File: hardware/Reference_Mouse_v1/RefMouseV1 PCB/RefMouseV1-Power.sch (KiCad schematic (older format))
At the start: 9 parts, among them U1 TPS6205X

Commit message: More reference mouse pcb stuff
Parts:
- added JP2: M02PTH, SparkFun-1X02, symbol M02PTH
- added TP3: TEST-POINT3X5, SparkFun-PAD.03X.05, symbol TEST-POINT3X5
- gave numbers to parts that had none: 3
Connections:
- wire segments 42 -> 37
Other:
- note added: "+3.3V test point"
- note added: "0.1" header footprint for alternate\nconnectors, measurement, or charging."
- note added: "Always-on battery voltage"
- note added: "Bend and solder a clipped component lead here\nfor use as an alligator-clipable GND test point."
- note added: "Main power switch.\nEnables main regulators and\nmotor drivers. Does not need to\nbe rated for very much current."
- note added: "Mechanically switched battery voltage.\nNot for high-current loads."
- note added: "Polarized JST-XH\nLiPo balance connector"
- note added: "Regulated high-current 3.3V supply"
- moved on the sheet: M1
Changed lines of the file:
@@
 Sheet 2 2
 Title "TPS6205x-based Fixed Voltage Switching Regulator Module"
-Date "26 aug 2013"
+Date "30 aug 2013"
 Rev "A"
 Comp "UCR Micromouse"
@@
 $EndComp
 $Comp
-L GND #PWR08
+L GND #PWR03
 U 1 1 51E3374F
 P 2600 2500
-F 0 "#PWR08" H 2600 2500 30  0001 C CNN
+F 0 "#PWR03" H 2600 2500 30  0001 C CNN
 F 1 "GND" H 2600 2430 30  0001 C CNN
 F 2 "" H 2600 2500 60  0000 C CNN
@@
 $EndComp
 $Comp
-L GND #PWR09
+L GND #PWR04
 U 1 1 51E33C6A
 P 6150 2600
-F 0 "#PWR09" H 6150 2600 30  0001 C CNN
+F 0 "#PWR04" H 6150 2600 30  0001 C CNN
 F 1 "GND" H 6150 2530 30  0001 C CNN
 F 2 "" H 6150 2600 60  0000 C CNN
@@
 $EndComp
 $Comp
-L GND #PWR012
+L GND #PWR05
 U 1 1 51E34F59
 P 6450 3150
-F 0 "#PWR012" H 6450 3150 30  0001 C CNN
+F 0 "#PWR05" H 6450 3150 30  0001 C CNN
 F 1 "GND" H 6450 3080 30  0001 C CNN
 F 2 "" H 6450 3150 60  0000 C CNN
@@
 NoConn ~ 5100 2700
 $Comp
-L SWITCH-SPSTPTH S?
+L SWITCH-SPSTPTH S1
 U 1 1 521A8FC9
 P 2200 3700
-F 0 "S?" H 2150 3950 50  0000 L BNN
+F 0 "S1" H 2150 3950 50  0000 L BNN
 F 1 "SWITCH-SPSTPTH" H 2150 3450 50  0000 L BNN
 F 2 "SparkFun-SWITCH-SPDT" H 2500 3400 50  0001 C CNN
@@
 $EndComp
 $Comp
-L BATTBALANCE-2S M?
+L BATTBALANCE-2S M1
 U 1 1 521AAB8A
-P 900 2200
-F 0 "M?" H 800 2400 60  0000 C CNN
-F 1 "BATTBALANCE-2S" H 1125 1975 60  0000 C CNN
-F 2 "" H 950 2200 60  0000 C CNN
-F 3 "" H 950 2200 60  0000 C CNN
-	1    900  2200
-	1    0    0    -1
-$EndComp
-$Comp
-L GND #PWR?
+P 950 2200
+F 0 "M1" H 850 2400 60  0000 C CNN
+F 1 "BATTBALANCE-2S" H 1175 1975 60  0000 C CNN
+F 2 "" H 1000 2200 60  0000 C CNN
+F 3 "" H 1000 2200 60  0000 C CNN
+	1    950  2200
+	1    0    0    -1
+$EndComp
+$Comp
+L GND #PWR06
 U 1 1 521AABA6
 P 1600 2500
-F 0 "#PWR?" H 1600 2500 30  0001 C CNN
+F 0 "#PWR06" H 1600 2500 30  0001 C CNN
 F 1 "GND" H 1600 2430 30  0001 C CNN
 F 2 "" H 1600 2500 60  0000 C CNN
@@
 	1    0    0    -1
 $EndComp
-Wire Wire Line
-	5100 2100 5250 2100
-Wire Wire Line
-	3000 2300 3500 2300
-Wire Wire Line
-	5100 2500 5400 2500
-Wire Wire Line
-	5100 2300 5950 2300
-Wire Wire Line
-	3250 2700 3500 2700
-Wire Wire Line
-	3250 2500 3250 2700
-Wire Wire Line
-	3250 2700 3250 3200
-Wire Wire Line
-	3250 3200 4200 3200
-Wire Wire Line
-	4200 3200 4400 3200
-Wire Wire Line
-	4400 3200 5400 3200
-Wire Wire Line
-	5400 3200 5400 2500
-Connection ~ 4400 3200
-Connection ~ 4200 3200
-Wire Wire Line
-	4200 3200 4200 3350
-Connection ~ 2600 2100
-Wire Wire Line
-	6150 2500 6150 2600
-Connection ~ 6150 2100
-Wire Wire Line
-	1400 2100 1400 2100
-Wire Wire Line
-	1400 2100 1900 2100
-Wire Wire Line
-	1900 2100 2600 2100
-Wire Wire Line
-	2600 2100 3500 2100
-Wire Wire Line
-	3250 2500 3500 2500
-Wire Wire Line
-	5850 2100 5950 2100
-Wire Wire Line
-	5950 2100 6150 2100
-Wire Wire Line
-	6150 2100 6450 2100
-Wire Wire Line
-	6450 2100 6900 2100
-Wire Wire Line
-	5950 2300 5950 2100
-Connection ~ 5950 2100
-Wire Wire Line
-	6450 3150 6450 3100
-Wire Wire Line
-	6450 2700 6450 2650
-Wire Wire Line
-	6450 2150 6450 2100
-Connection ~ 6450 2100
-Connection ~ 3250 2700
-Wire Wire Line
-	1400 2300 1600 2300
-Wire Wire Line
-	1600 1700 1600 2300
-Wire Wire Line
-	1600 2300 1600 2500
-Wire Wire Line
-	2000 3600 1900 3600
-Wire Wire Line
-	1900 3600 1900 2100
-Connection ~ 1900 2100
-$Comp
-L GND #PWR?
+$Comp
+L GND #PWR07
 U 1 1 521AACDE
 P 1500 4050
-F 0 "#PWR?" H 1500 4050 30  0001 C CNN
+F 0 "#PWR07" H 1500 4050 30  0001 C CNN
 F 1 "GND" H 1500 3980 30  0001 C CNN
 F 2 "" H 1500 4050 60  0000 C CNN
@@
 	1    0    0    -1
 $EndComp
-Wire Wire Line
-	2000 3800 1500 3800
-Wire Wire Line
-	1500 3800 1500 4050
-Wire Wire Line
-	2300 3700 3000 3700
-Wire Wire Line
-	3000 3700 3200 3700
 Text Label 2400 3700 0    60   ~ 0
 VBATT_SW
-Wire Wire Line
-	3000 3700 3000 2300
-Connection ~ 3000 3700
-$Comp
-L M03PTH JP?
+$Comp
+L M03PTH JP1
 U 1 1 521ABBD8
 P 950 1600
-F 0 "JP?" H 850 1830 50  0000 L BNN
+F 0 "JP1" H 850 1830 50  0000 L BNN
 F 1 "M03PTH" H 850 1300 50  0000 L BNN
 F 2 "SparkFun-1X03" H 950 1750 50  0001 C CNN
@@
 	1    0    0    -1
 $EndComp
-Wire Wire Line
-	1250 1700 1600 1700
-Connection ~ 1600 2300
-Wire Wire Line
-	1250 1600 1500 1600
-Wire Wire Line
-	1500 1600 1500 2200
-Wire Wire Line
-	1500 2200 1400 2200
-Wire Wire Line
-	1250 1500 1400 1500
-Wire Wire Line
-	1400 1500 1400 2100
-Connection ~ 1400 2100
 Text HLabel 3200 3700 2    60   Input ~ 0
 VBATT_SW
 Text HLabel 6900 2100 2    60   Input ~ 0
 +3.3V
+Text HLabel 3300 1500 2    60   Input ~ 0
+VBATT
+Text Notes 3350 1650 0    60   ~ 0
+Always-on battery voltage
+Text Notes 3250 3850 0    60   ~ 0
+Mechanically switched battery voltage.\nNot for high-current loads.
+Text Notes 7000 2250 0    60   ~ 0
+Regulated high-current 3.3V supply
+Text Notes 600  2600 0    60   ~ 0
+Polarized JST-XH\nLiPo balance connector
+Text Notes 650  1150 0    60   ~ 0
+0.1" header footprint for alternate\nconnectors, measurement, or charging.
+Text Notes 1800 4100 0    60   ~ 0
+Main power switch.\nEnables main regulators and\nmotor drivers. Does not need to\nbe rated for very much current.
+$Comp
+L TEST-POINT3X5 TP3
+U 1 1 52208851
+P 6700 1750
+F 0 "TP3" H 6800 1850 50  0000 C CNN
+F 1 "TEST-POINT3X5" H 6800 1650 50  0000 C CNN
+F 2 "SparkFun-PAD.03X.05" H 6800 1550 50  0001 C CNN
+F 3 "" H 6700 1750 60  0000 C CNN
+	1    6700 1750
+	1    0    0    -1
+$EndComp
+Wire Wire Line
+	6450 1750 6700 1750
+Connection ~ 3000 2100
+Wire Wire Line
+	3000 1500 3300 1500
+Wire Wire Line
+	3000 2100 3000 1500
+Connection ~ 1400 2100
+Wire Wire Line
+	1400 1500 1400 2100
+Wire Wire Line
+	1250 1500 1400 1500
+Wire Wire Line
+	1500 2200 1400 2200
+Wire Wire Line
+	1500 1600 1500 2200
+Wire Wire Line
+	1250 1600 1500 1600
+Connection ~ 1600 2300
+Wire Wire Line
+	1250 1700 1600 1700
+Connection ~ 3000 3700
+Wire Wire Line
+	3000 3700 3000 2300
+Wire Wire Line
+	2300 3700 3200 3700
+Wire Wire Line
+	1500 3800 1500 4050
+Wire Wire Line
+	2000 3800 1500 3800
+Connection ~ 1900 2100
+Wire Wire Line
+	1900 3600 1900 2100
+Wire Wire Line
+	2000 3600 1900 3600
+Wire Wire Line
+	1600 1700 1600 2500
+Wire Wire Line
+	1400 2300 1600 2300
+Connection ~ 3250 2700
+Connection ~ 6450 2100
+Wire Wire Line
+	6450 1750 6450 2150
+Wire Wire Line
+	6450 2700 6450 2650
+Wire Wire Line
+	6450 3150 6450 3100
+Connection ~ 5950 2100
+Wire Wire Line
+	5950 2300 5950 2100
+Wire Wire Line
+	5850 2100 6900 2100
+Wire Wire Line
+	3250 2500 3500 2500
+Wire Wire Line
+	1400 2100 3500 2100
+Connection ~ 6150 2100
+Wire Wire Line
+	6150 2500 6150 2600
+Connection ~ 2600 2100
+Wire Wire Line
+	4200 3200 4200 3350
+Connection ~ 4200 3200
+Connection ~ 4400 3200
+Wire Wire Line
+	5400 3200 5400 2500
+Wire Wire Line
+	3250 3200 5400 3200
+Wire Wire Line
+	3250 2500 3250 3200
+Wire Wire Line
+	3250 2700 3500 2700
+Wire Wire Line
+	5100 2300 5950 2300
+Wire Wire Line
+	5400 2500 5100 2500
+Wire Wire Line
+	3000 2300 3500 2300
+Wire Wire Line
+	5100 2100 5250 2100
+$Comp
+L M02PTH JP2
+U 1 1 522088E4
+P 7750 3050
+F 0 "JP2" H 7650 3280 50  0000 L BNN
+F 1 "M02PTH" H 7650 2850 50  0000 L BNN
+F 2 "SparkFun-1X02" H 7750 3200 50  0001 C CNN
+F 3 "" H 7750 3050 60  0000 C CNN
+	1    7750 3050
+	-1   0    0    1
+$EndComp
+$Comp
+L GND #PWR08
+U 1 1 522088F1
+P 7400 3300
+F 0 "#PWR08" H 7400 3300 30  0001 C CNN
+F 1 "GND" H 7400 3230 30  0001 C CNN
+F 2 "" H 7400 3300 60  0000 C CNN
+F 3 "" H 7400 3300 60  0000 C CNN
+	1    7400 3300
+	1    0    0    -1
+$EndComp
+Wire Wire Line
+	7450 3050 7400 3050
+Wire Wire Line
+	7400 3050 7400 3300
+Wire Wire Line
+	7450 3150 7400 3150
+Connection ~ 7400 3150
+Text Notes 7950 3100 0    60   ~ 0
+Bend and solder a clipped component lead here\nfor use as an alligator-clipable GND test point.
+Text Notes 6650 1550 0    60   ~ 0
++3.3V test point
 $EndSCHEMATC

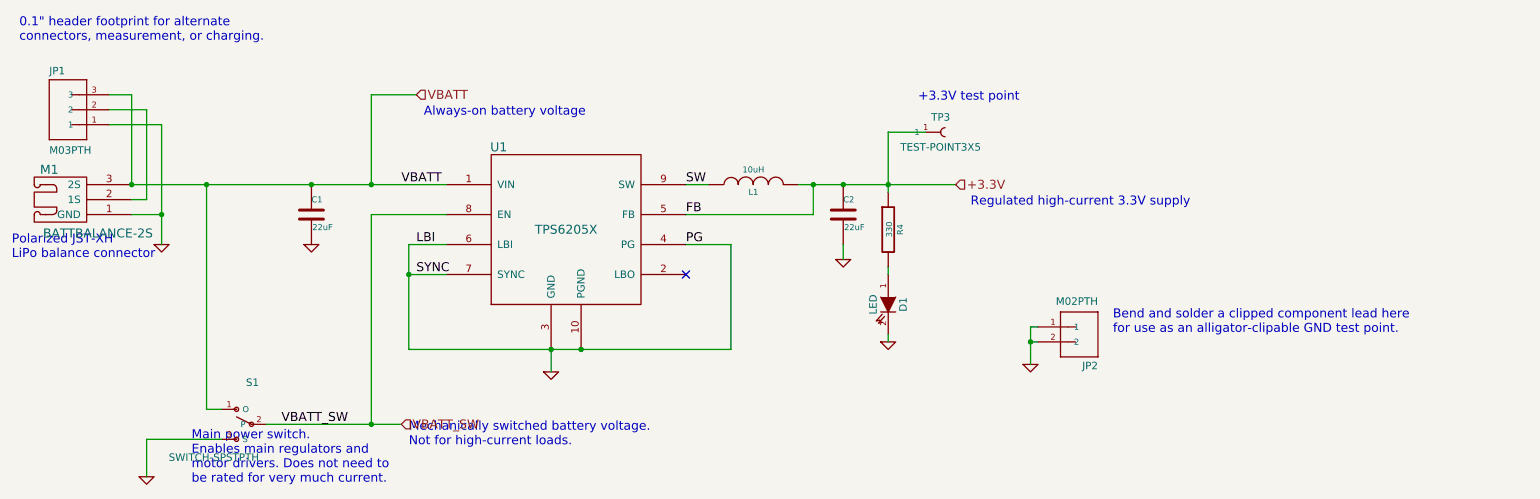
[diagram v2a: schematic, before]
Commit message: Added DRV sch symbol and motor sub-schematic.
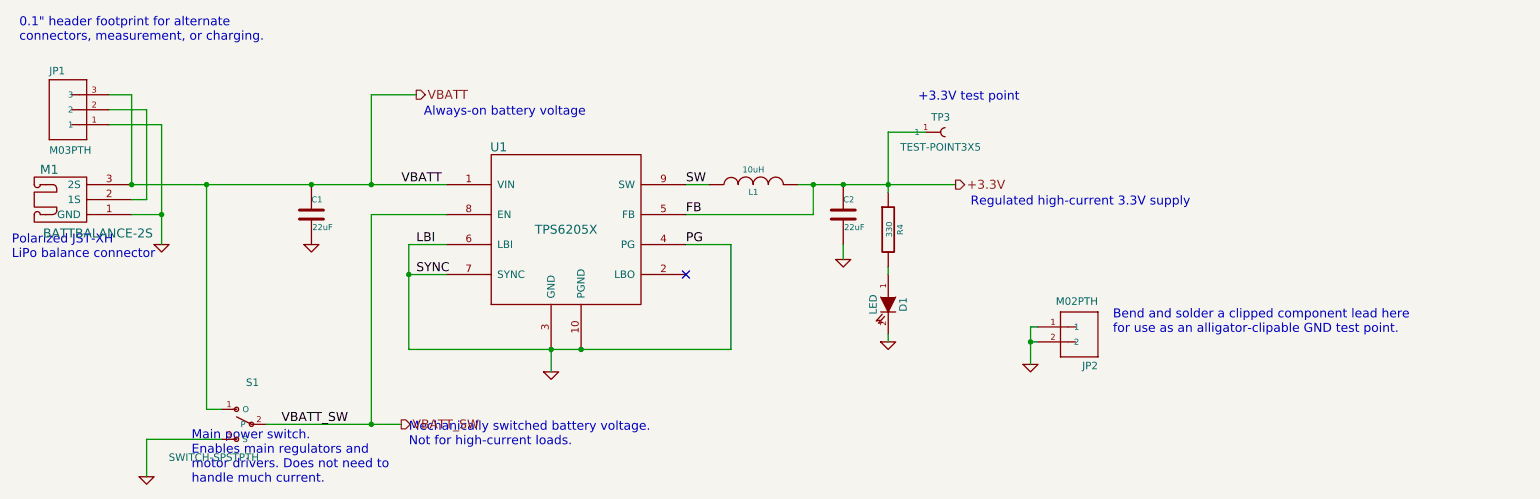
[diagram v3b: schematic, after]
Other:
- note added: "Main power switch.\nEnables main regulators and\nmotor drivers. Does not need to\nhandle much current."
- note removed: "Main power switch.\nEnables main regulators and\nmotor drivers. Does not need to\nbe rated for very much current."
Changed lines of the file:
@@
 EESchema Schematic File Version 2
+LIBS:power
+LIBS:device
+LIBS:transistors
+LIBS:conn
+LIBS:linear
+LIBS:regul
+LIBS:74xx
+LIBS:cmos4000
+LIBS:adc-dac
+LIBS:memory
+LIBS:xilinx
+LIBS:special
+LIBS:microcontrollers
+LIBS:dsp
+LIBS:microchip
+LIBS:analog_switches
+LIBS:motorola
+LIBS:texas
+LIBS:intel
+LIBS:audio
+LIBS:interface
+LIBS:digital-audio
+LIBS:philips
+LIBS:display
+LIBS:cypress
+LIBS:siliconi
+LIBS:opto
+LIBS:atmel
+LIBS:contrib
+LIBS:valves
 LIBS:stm32f103rx
 LIBS:SparkFun
 LIBS:tps6205x
 LIBS:JST-XH-BattBalance
+LIBS:drv8837
 LIBS:RefMouseV1-cache
 EELAYER 27 0
@@
 $Descr USLetter 11000 8500
 encoding utf-8
-Sheet 2 2
+Sheet 2 3
 Title "TPS6205x-based Fixed Voltage Switching Regulator Module"
-Date "22 sep 2013"
+Date "5 sep 2013"
 Rev "A"
 Comp "UCR Micromouse"
@@
 	1    0    0    -1
 $EndComp
-Text HLabel 3200 3700 2    60   Input ~ 0
+Text HLabel 3200 3700 2    60   Output ~ 0
 VBATT_SW
-Text HLabel 6900 2100 2    60   Input ~ 0
+Text HLabel 6900 2100 2    60   Output ~ 0
 +3.3V
-Text HLabel 3300 1500 2    60   Input ~ 0
+Text HLabel 3300 1500 2    60   Output ~ 0
 VBATT
 Text Notes 3350 1650 0    60   ~ 0
@@
 0.1" header footprint for alternate\nconnectors, measurement, or charging.
 Text Notes 1800 4100 0    60   ~ 0
-Main power switch.\nEnables main regulators and\nmotor drivers. Does not need to\nbe rated for very much current.
+Main power switch.\nEnables main regulators and\nmotor drivers. Does not need to\nhandle much current.
 $Comp
 L TEST-POINT3X5 TP3
